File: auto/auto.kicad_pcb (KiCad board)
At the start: 2 copper layers, 2 parts, among them U2 module_mpu6050

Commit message: esquematico(falta agregar fusible 1 / 2 A)
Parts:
- added J1: BATERIAS_PC, Connector_PinHeader_2.54mm:PinHeader_1x02_P2.54mm_Vertical, F.Cu at (91.3, 141.0)
- added J2: BATERIA_AUTO, terminals_bateries:teminals_bateries, F.Cu at (108.9, 109.6)
- added J3: servo, Connector_PinHeader_2.54mm:PinHeader_1x03_P2.54mm_Vertical, F.Cu at (82.1, 141.0)
- added J4: BOCINA, Connector_PinHeader_2.54mm:PinHeader_1x02_P2.54mm_Vertical, F.Cu at (95.9, 141.0)
- added Q1: 2N3904, Package_TO_SOT_THT:TO-92_Inline, F.Cu at (174.9, 127.8)
- added Q2: 2N3904, Package_TO_SOT_THT:TO-92_Inline, F.Cu at (174.9, 133.6)
- added R1: 10K, Resistor_THT:R_Axial_DIN0204_L3.6mm_D1.6mm_P5.08mm_Horizontal, F.Cu at (180.5, 43.6)
- added R2: 10k, Resistor_THT:R_Axial_DIN0204_L3.6mm_D1.6mm_P5.08mm_Horizontal, F.Cu at (180.5, 46.8)
- added R3: 10k, Resistor_THT:R_Axial_DIN0204_L3.6mm_D1.6mm_P5.08mm_Horizontal, F.Cu at (180.5, 49.9)
- added R4: 10k, Resistor_THT:R_Axial_DIN0204_L3.6mm_D1.6mm_P5.08mm_Horizontal, F.Cu at (180.5, 53.1)
- added R5: 10k, Resistor_THT:R_Axial_DIN0204_L3.6mm_D1.6mm_P5.08mm_Horizontal, F.Cu at (180.5, 56.2)
- added R6: 10k, Resistor_THT:R_Axial_DIN0204_L3.6mm_D1.6mm_P5.08mm_Horizontal, F.Cu at (180.5, 59.4)
- added R7: 10K, Resistor_THT:R_Axial_DIN0204_L3.6mm_D1.6mm_P5.08mm_Horizontal, F.Cu at (180.5, 62.5)
- added R8: 10k, Resistor_THT:R_Axial_DIN0204_L3.6mm_D1.6mm_P5.08mm_Horizontal, F.Cu at (180.5, 65.7)
- added SW1: SW_DPST_x2, Button_Switch_THT:SW_DIP_SPSTx01_Slide_6.7x4.1mm_W7.62mm_P2.54mm_LowProfile, F.Cu at (174.5, 145.0)
- added SW2: SW1, Button_Switch_THT:SW_PUSH-12mm_Wuerth-430476085716, F.Cu at (135.9, 102.5)
- added SW3: SW_DPST_x2, Button_Switch_THT:SW_PUSH-12mm_Wuerth-430476085716, F.Cu at (135.9, 116.1)
- added SW4: SW_DPST_x2, Button_Switch_THT:SW_PUSH-12mm_Wuerth-430476085716, F.Cu at (135.9, 129.6)
- added U3: ~, Modulos_desafio_eco:tft_3.5_display, F.Cu at (90.4, 70.2)
- added U4: ~, my_esp32:esp32, F.Cu at (112.2, 130.4)
- added U6: L7805, Package_TO_SOT_THT:TO-220-3_Vertical, F.Cu at (176.1, 140.1)
- added U7: ~, Connector_PinHeader_2.54mm:PinHeader_1x03_P2.54mm_Vertical, F.Cu at (86.7, 141.0)
- added U8: ~, LORA:SHIELD XL1278, F.Cu at (172.2, 125.3)
- U1: footprint my_esp32:esp32 -> GY-NEO6MV2:GY-NEO6MV2
- moved U2 72.5 mm to (181.3, 69.6)
- moved U1 42.0 mm to (186.2, 123.8)
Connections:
- U1 pad 1: unconnected-(U1-3.3V-Pad1) -> VCC
- U1 pad 2: unconnected-(U1-EN-Pad2) -> RX_GPS
- U1 pad 3: unconnected-(U1-GPIO36-Pad3) -> TX_GPS
- U1 pad 4: unconnected-(U1-GPIO39-Pad4) -> GND
- U2 pad 1: unconnected-(U2-VCC-Pad1) -> VCC
- U2 pad 2: unconnected-(U2-GND-Pad2) -> GND
- U2 pad 3: unconnected-(U2-SCL-Pad3) -> SCL_MPU
- U2 pad 4: unconnected-(U2-SDA-Pad4) -> SDA_MPU

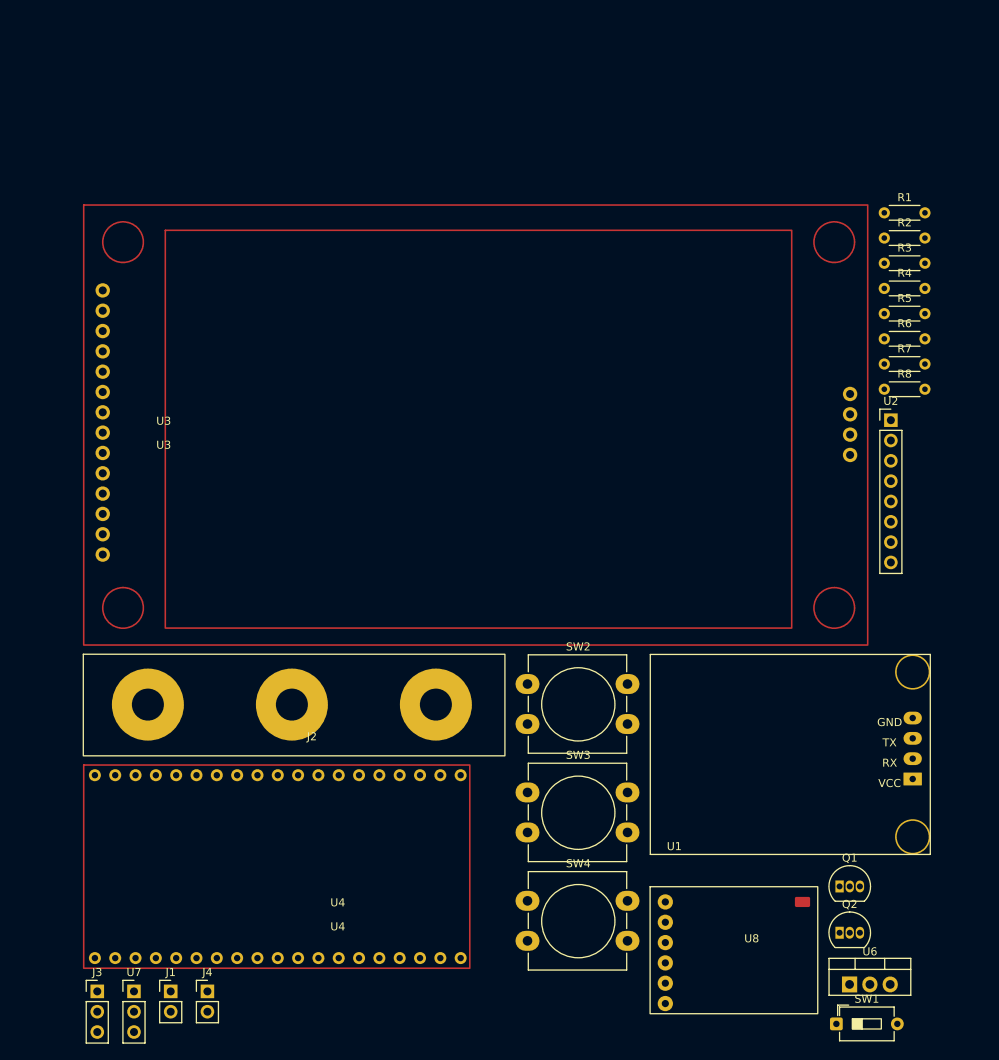
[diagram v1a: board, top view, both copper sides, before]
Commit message: esquematico finalizado, PCB en proceso.
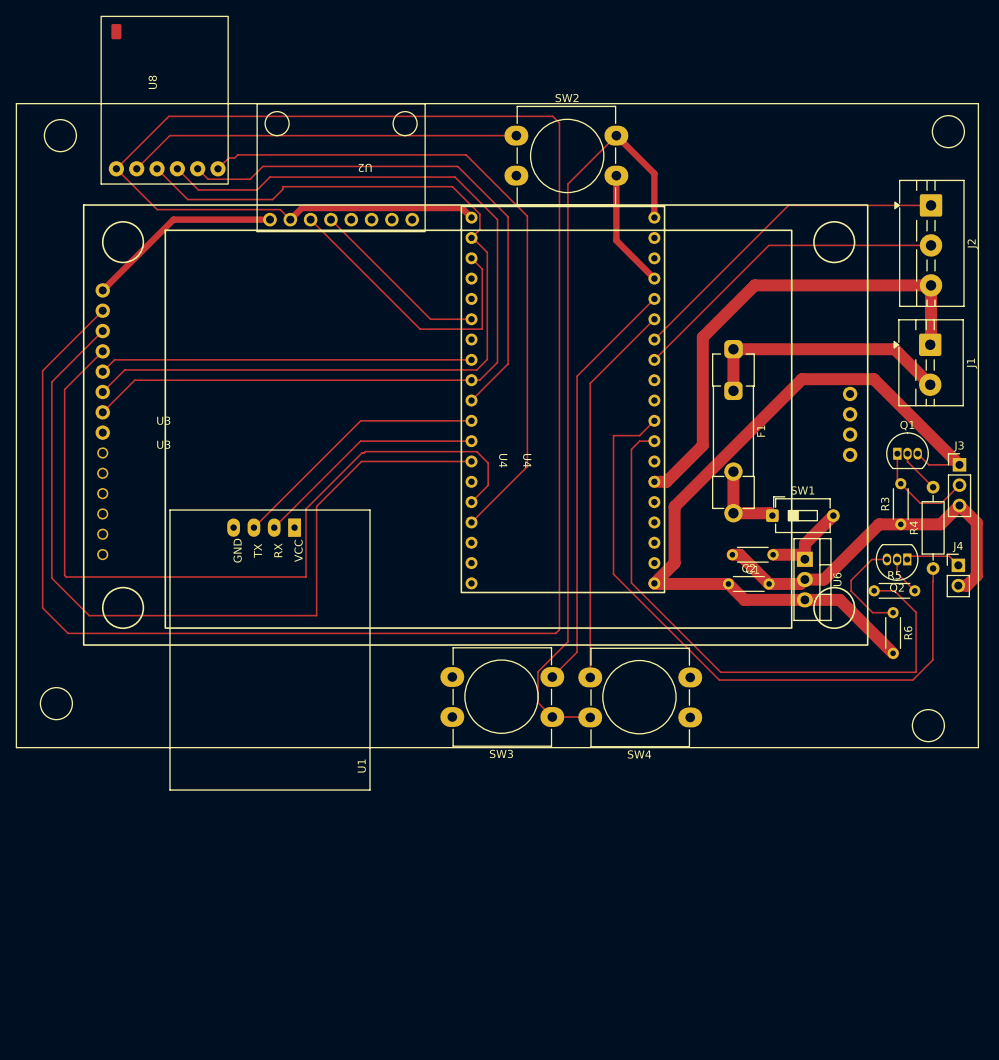
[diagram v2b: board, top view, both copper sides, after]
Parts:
- removed R1, R7: 10K, Resistor_THT:R_Axial_DIN0204_L3.6mm_D1.6mm_P5.08mm_Horizontal
- removed R2, R8: 10k, Resistor_THT:R_Axial_DIN0204_L3.6mm_D1.6mm_P5.08mm_Horizontal
- removed U7: ~, Connector_PinHeader_2.54mm:PinHeader_1x03_P2.54mm_Vertical
- added C1: 1uF, Resistor_THT:R_Axial_DIN0204_L3.6mm_D1.6mm_P5.08mm_Horizontal, F.Cu at (166.6, 86.4)
- added C2: 0.33uF, Resistor_THT:R_Axial_DIN0204_L3.6mm_D1.6mm_P5.08mm_Horizontal, F.Cu at (161.0, 90.0)
- added F1: Fuse, Fuse:Fuseholder_Clip-5x20mm_Littelfuse_445-030_Inline_P20.50x5.20mm_D1.30mm_Horizontal, F.Cu at (161.6, 60.7)
- J1: footprint Connector_PinHeader_2.54mm:PinHeader_1x02_P2.54mm_Vertical -> TerminalBlock:TerminalBlock_MaiXu_MX126-5.0-02P_1x02_P5.00mm
- J2: value BATERIA_AUTO -> Cableado_hacia_auto; footprint terminals_bateries:teminals_bateries -> TerminalBlock:TerminalBlock_MaiXu_MX126-5.0-03P_1x03_P5.00mm
- R4: footprint Resistor_THT:R_Axial_DIN0204_L3.6mm_D1.6mm_P5.08mm_Horizontal -> Resistor_THT:R_Axial_DIN0207_L6.3mm_D2.5mm_P10.16mm_Horizontal
- U2: footprint Connector_PinHeader_2.54mm:PinHeader_1x08_P2.54mm_Vertical -> MPU6050:module_MPU6050
- moved U8 140.6 mm to (80.1, 19.1), turned to 90 degrees
- moved J3 126.3 mm to (189.9, 75.2)
- moved J1 124.7 mm to (186.2, 60.1), turned to -90 degrees
- moved J4 107.9 mm to (189.7, 87.7)
- moved J2 102.3 mm to (186.3, 42.7), turned to -90 degrees
- moved U1 82.2 mm to (116.2, 80.8), turned to 90 degrees
- moved U2 70.5 mm to (119.1, 36.5), turned to 90 degrees
- moved SW2 68.6 mm to (134.5, 34.0)
- moved SW1 64.0 mm to (166.5, 81.5)
- moved U4 60.4 mm to (135.3, 74.6), turned to -90 degrees
- moved Q1 54.6 mm to (182.1, 73.8)
- moved U6 53.4 mm to (170.6, 87.0), turned to -90 degrees
- moved Q2 47.4 mm to (183.4, 87.0), turned to 180 degrees
- moved R4 35.5 mm to (186.6, 88.1), turned to 90 degrees
- moved R5 34.7 mm to (179.2, 90.9)
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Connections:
- J2 pad 1: VBAT_OUT -> VBAT_U
- J2 pad 2: GND -> ACS
- J2 pad 3: VBAT+ -> GND
- SW1 pad 1: Net-(J1-Pin_2) -> Net-(SW1A-A)
- U3 pad 8: LED_TFT -> 3.3V
- U4 pad 11: LED_TFT -> Servo_C
- U4 pad 14: unconnected-(U4-GND-Pad14) -> GND
- U4 pad 26: unconnected-(U4-GND-Pad26) -> GND
- U4 pad 3: ACS -> unconnected-(U4-GPIO36-Pad3)
- U4 pad 34: RST_Lora -> RST_TFT
- U4 pad 35: RST_TFT -> RST_Lora
- U4 pad 8: unconnected-(U4-GPIO33-Pad8) -> ACS
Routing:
- net GND: track 0.00 -> 383.2 mm
- net 3.3V: track 0.00 -> 143.6 mm
- net VCC: track 0.00 -> 121.1 mm
- net SCK_Lora_TFT: track 0.00 -> 113.8 mm
- net MOSI_Lora_TFT: track 0.00 -> 113.5 mm
- net CS_TFT: track 0.00 -> 104.0 mm
- net RST_TFT: track 0.00 -> 100.8 mm
- net RST_Lora: track 0.00 -> 83.7 mm
- net Servo_C: track 0.00 -> 81.1 mm
- net Bocina_C: track 0.00 -> 74.0 mm
- net CS_Lora: track 0.00 -> 67.5 mm
- net Option2: track 0.00 -> 52.5 mm
- net Option3: track 0.00 -> 48.1 mm
- net DC_TFT: track 0.00 -> 46.7 mm
- net VBAT_U: track 0.00 -> 41.5 mm
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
